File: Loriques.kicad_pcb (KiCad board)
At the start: 6 copper layers, 144.8 x 106.7 mm, 123 parts, among them IC10 MAX17263LETD+T, IC12 TPS22975, IC19 TPS22975, IC2 MCP73871, IC4 TPS2013A, IC6 SN74LVC244A, IC7 LP38691-ADJ, IC9 LTC3113, J1 JST_PH_3PIN, J2 JST_4PIN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

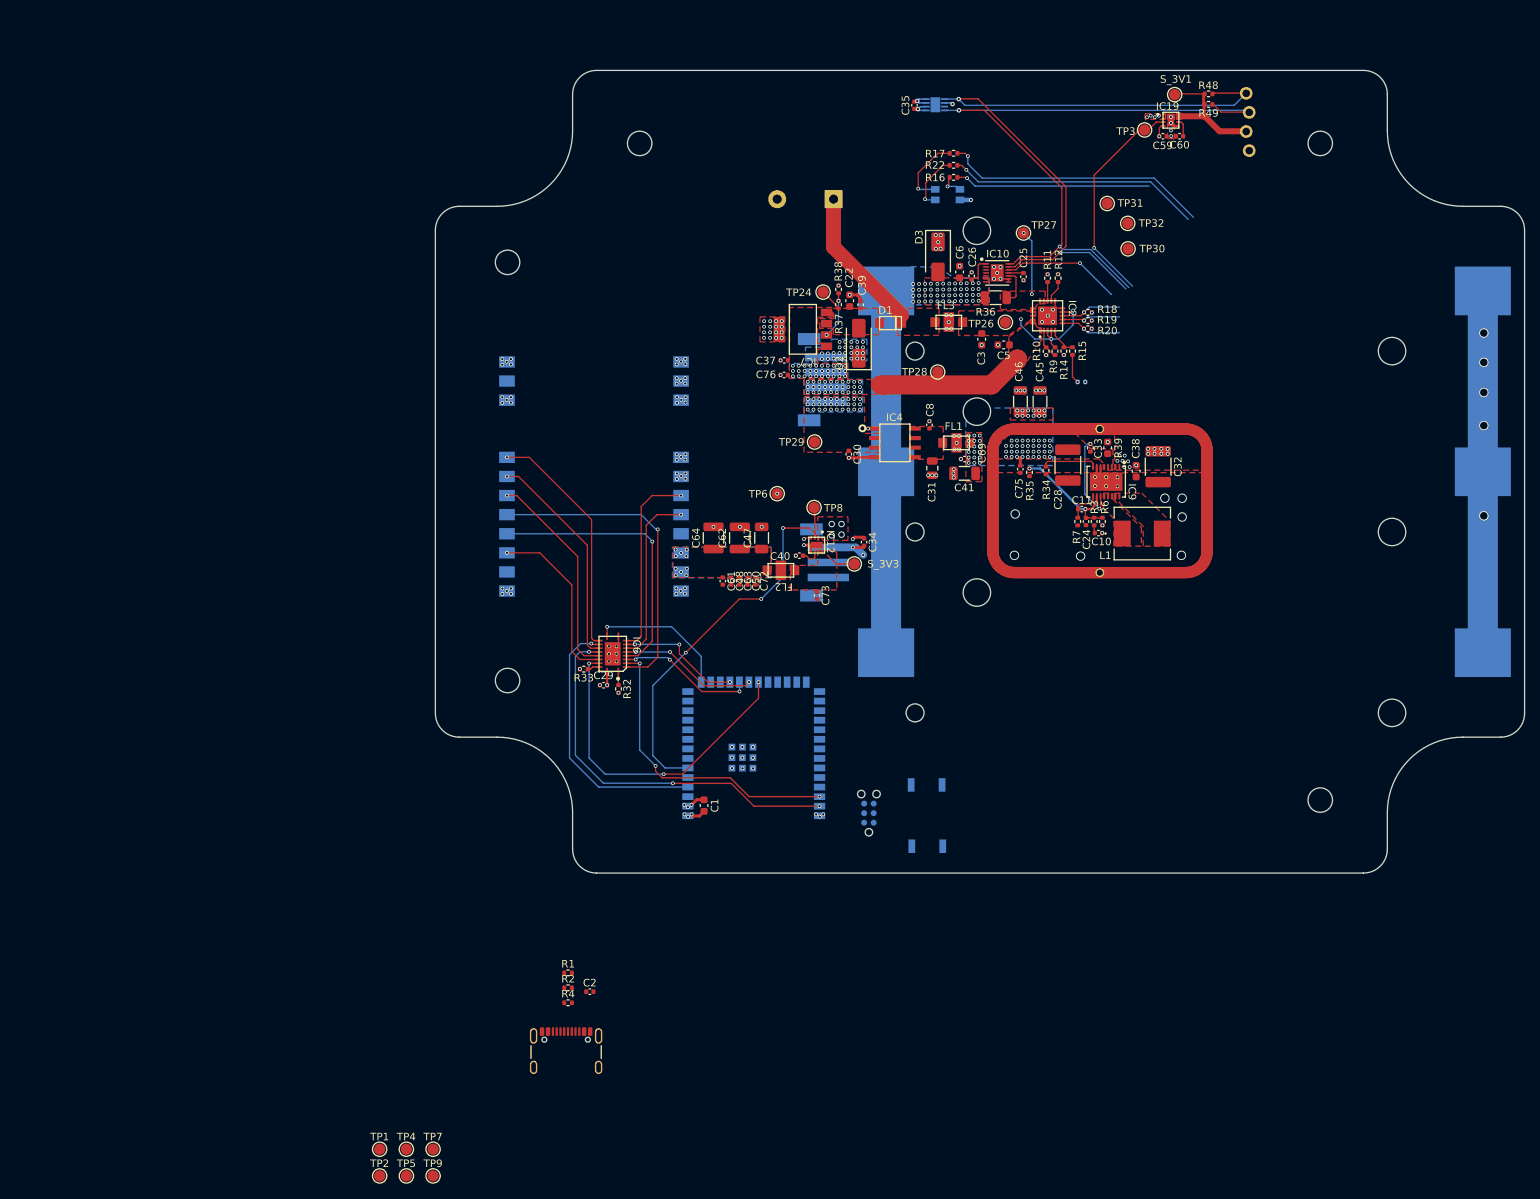
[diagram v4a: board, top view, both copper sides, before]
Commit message: initial routing done!
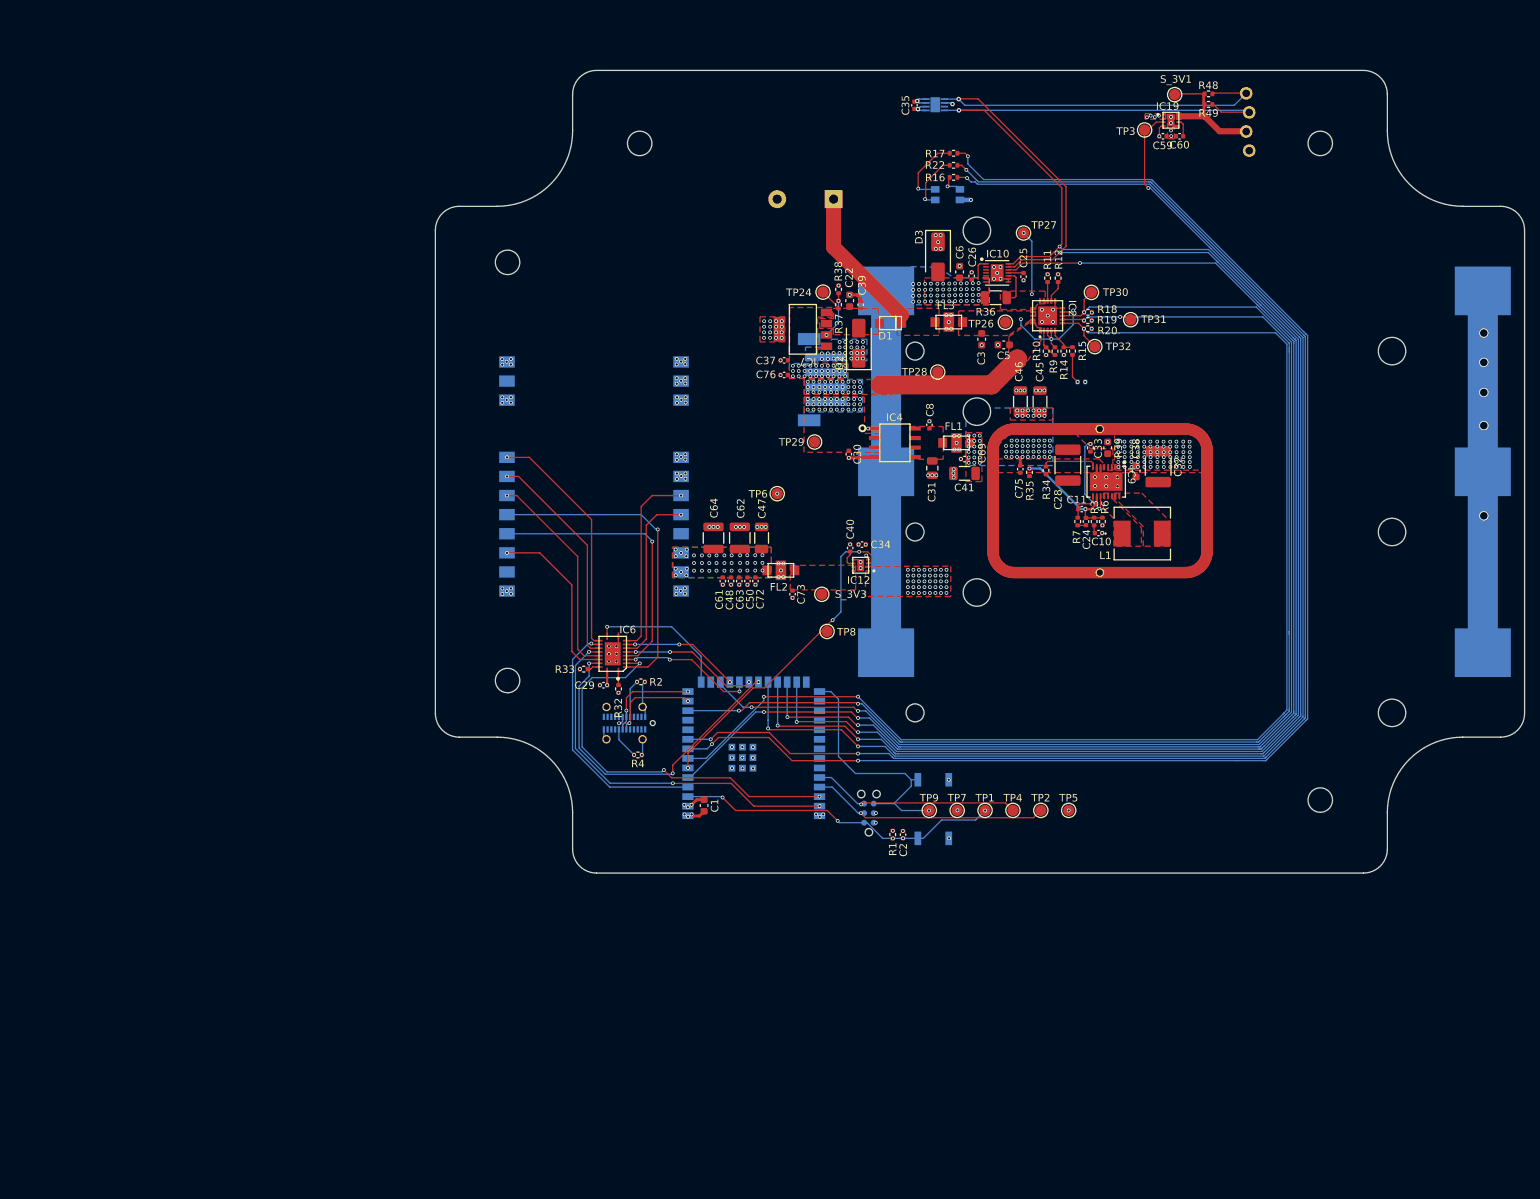
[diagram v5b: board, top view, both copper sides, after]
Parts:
- removed J1: JST_PH_3PIN, Loriques:JST-PH-3-SMT
- J7: footprint Loriques:USB_C_Receptacle_GCT_USB4105-xx-A -> Loriques:CONN_12402032E202A_AMP; moved to B.Cu
- moved TP5 100.6 mm to (160.3, 150.0)
- moved TP2 100.4 mm to (156.6, 150.0)
- moved TP4 92.4 mm to (152.9, 150.0)
- moved TP1 92.2 mm to (149.2, 150.0)
- moved TP7 83.0 mm to (145.5, 150.0)
- moved TP9 81.9 mm to (141.8, 150.0)
- moved R1 46.9 mm to (136.9, 153.2), turned to 90 degrees
- moved C2 46.6 mm to (138.3, 153.3), turned to 90 degrees
- moved J7 45.4 mm to (101.2, 138.4), turned to 180 degrees
- moved R2 41.8 mm to (103.4, 132.9), turned to 180 degrees
- moved R4 34.2 mm to (103.0, 142.7), turned to 180 degrees
- moved TP32 17.0 mm to (163.8, 88.4)
- moved TP8 16.6 mm to (128.2, 126.2)
- moved TP31 15.8 mm to (168.5, 84.8)
- moved TP30 7.57 mm to (163.3, 81.2)
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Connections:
- U1 pad 23: unconnected-(U1-GPIO21-Pad23) -> /MCU/DISP_EN
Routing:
- net /FUEL: track 15.8 -> 180.0 mm, vias 1 -> 3
- net /MCU/PG: track 8.14 -> 170.2 mm, vias 1 -> 3
- net /MCU/LED0R: track 25.8 -> 186.0 mm, vias 1 -> 3
- net /MCU/LED0G: track 35.4 -> 194.7 mm, vias 1 -> 3
- net /MCU/LED0B: track 33.5 -> 192.4 mm, vias 1 -> 3
- net /MCU/STAT2: track 7.87 -> 166.6 mm, vias 1 -> 4
- net /MCU/STAT1: track 8.10 -> 166.4 mm, vias 1 -> 3
- net /SDA: track 92.4 -> 243.6 mm, vias 2 -> 4
- net /SCL: track 90.9 -> 241.9 mm, vias 2 -> 4
- net /MCU/DISP_EN: track 29.1 -> 168.6 mm, vias 1 -> 3
- net /MCU/EN: track 0.00 -> 43.4 mm, vias 0 -> 5
- net /MCU/IO0: track 0.00 -> 34.3 mm, vias 0 -> 1
- net /MCU/P_TX: track 0.00 -> 32.0 mm, vias 0 -> 1
- net /MCU/P_RX: track 0.00 -> 28.0 mm, vias 0 -> 1
- net /MCU/USB_D-: track 0.00 -> 14.8 mm, vias 0 -> 3
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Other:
- board text added: "BOOT"
- board text added: "RESET"

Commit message: some DRC fixing
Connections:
- U1 pad 10: /MCU/TX_DEBUG_O -> unconnected-(U1-GPIO17/U1TXD/ADC2_CH6-Pad10)
- U1 pad 11: /MCU/RX_DEBUG_O -> unconnected-(U1-GPIO18/U1RXD/ADC2_CH7/CLK_OUT3-Pad11)

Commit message: silkscreen cleanup. add readme.
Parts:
- moved LED0 5.33 mm to (142.8, 63.0)
- moved R22 2.56 mm to (147.2, 64.6)
- moved R17 2.56 mm to (147.2, 61.4)
- moved R16 2.56 mm to (147.2, 63.0)
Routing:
- net Net-(LED0-G): track 9.53 -> 5.92 mm
- net Net-(LED0-R): track 3.07 -> 6.60 mm
- net /MCU/LED0G: track 194.7 -> 192.6 mm
- net Net-(LED0-B): track 7.65 -> 5.84 mm
- net /MCU/3V3: track 24.7 -> 23.3 mm
- net /MCU/LED0B: track 192.4 -> 190.9 mm
- net /MCU/LED0R: track 186.0 -> 184.6 mm
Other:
- board text removed: "DEBUG"
- board text removed: "gateway"
